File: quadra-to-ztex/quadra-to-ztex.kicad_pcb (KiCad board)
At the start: 4 copper layers, 100 x 100 mm, 33 parts, among them IC1 74CB3T16211DGGR, IC2 74CB3T16211DGGR, IC3 74CB3T16211DGGR, IC4 74CB3T16211DGGR, J1 Conn_02x07_Odd_Even, J2 10029449-111RLF (HDMI A), J3 A2541HWR-2x6P (Pmod 2x6 F R), U1 TPD12S016PWR, U14 8807-140-170LH

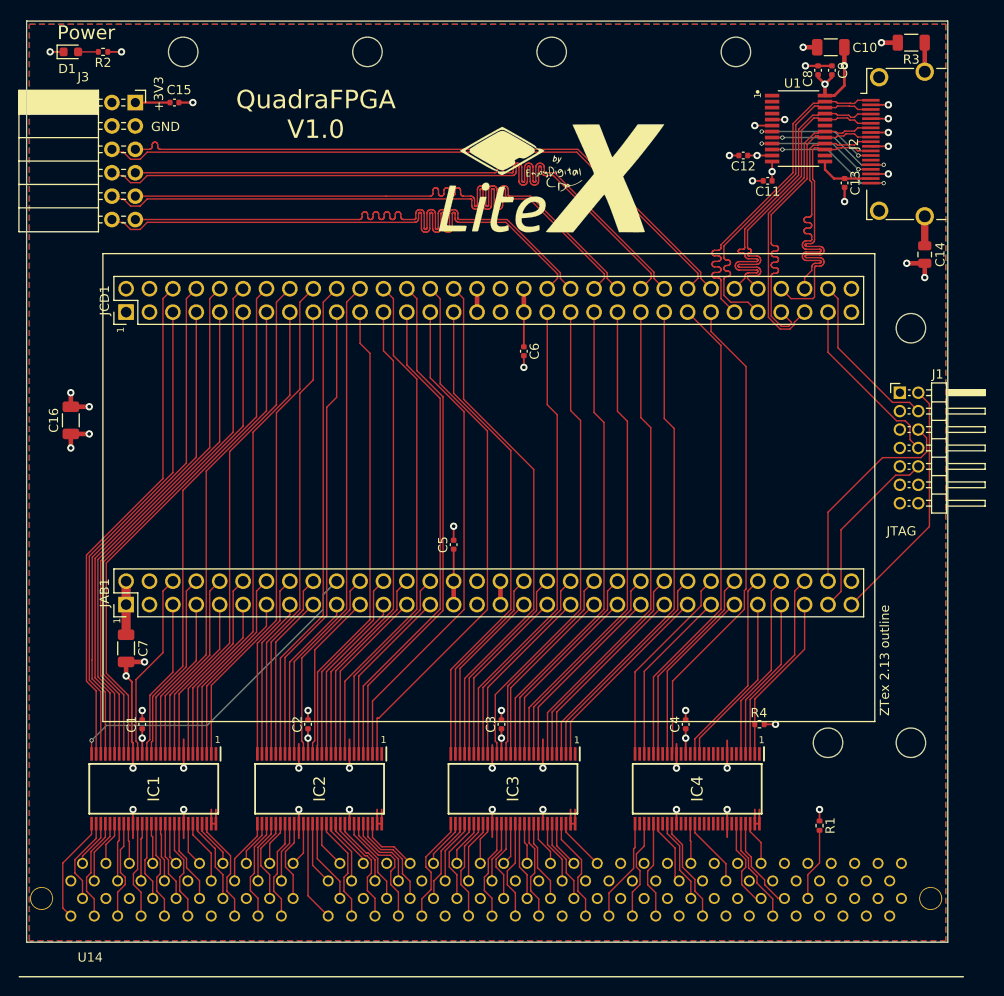
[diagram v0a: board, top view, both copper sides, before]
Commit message: R1 must be 0 ohm (there's a pull-up on the motherboard and it's stronger)
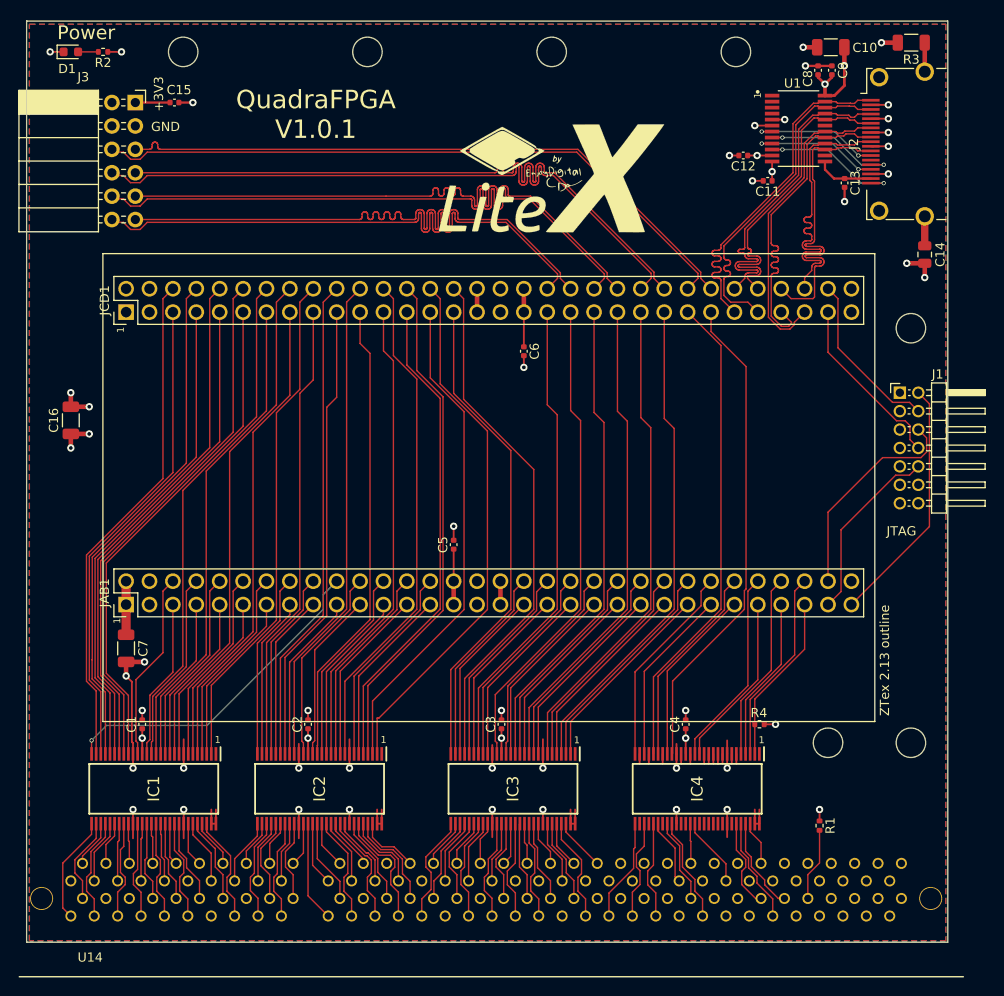
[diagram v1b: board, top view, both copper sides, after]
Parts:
- R1: value 10k -> 0
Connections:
- IC4 pad 10: (no net) -> GND
- IC4 pad 11: (no net) -> GND
- IC4 pad 12: (no net) -> GND
- IC4 pad 13: (no net) -> GND
- IC4 pad 16: (no net) -> GND
- IC4 pad 18: (no net) -> GND
- IC4 pad 22: (no net) -> GND
- IC4 pad 25: (no net) -> GND
- IC4 pad 27: (no net) -> GND
- IC4 pad 6: (no net) -> GND
- IC4 pad 7: (no net) -> GND
- IC4 pad 9: (no net) -> GND
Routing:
- net GND: track 109.4 -> 121.9 mm
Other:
- board text added: "QuadraFPGA V1.0.1"
- board text removed: "QuadraFPGA V1.0"
